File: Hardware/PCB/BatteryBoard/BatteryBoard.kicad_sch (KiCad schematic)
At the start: 16 parts

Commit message: wiring
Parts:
- added BT? (x2): BATT, symbol Device:Battery_Cell
- added C? (x2): 10u(3225), symbol Device:C_Small
- added C? (x2): 10u, symbol Device:C_Small
- added C?: 22u(3225), symbol Device:C_Small
- added C?: 4.7u, symbol Device:C_Small
- added C?: 47p, symbol Device:C_Small
- added C?: 0.047u, symbol Device:C_Small
- added C?: 0.47u, symbol Device:C_Small
- added D?: D_Schottky, symbol Device:D_Schottky
- added L?: 1uH, symbol Device:L_Small
- added R?: 330, symbol Device:R_Small
- added R? (x5): 4.7k, symbol Device:R_Small
- added R?: 10, symbol Device:R_Small
- added R?: 374, symbol Device:R_Small
- added U?: LT1963AEST-3.3, symbol Regulator_Linear:L7805
- added U?: NJM2396F05, symbol Regulator_extlib:NJM2396F05
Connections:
- net +BATT: now also U?.13 (BAT), U?.14 (BAT), BT?.1 (+), C?.1
- net GND: now also BT?.2 (-), C?.2, C?.2, C?.2, C?.2, C?.2, C?.2, C?.2, C?.2, R?.1, R?.1, U?.2 (GND), U?.3 (GND)
- net VBUS: now also R?.2, R?.2, R?.2, R?.2
- net PG: now reaches U?.1 (~{PG})
- net PG: now also R?.1
- net CBSET: now reaches U?.10 (CBSET)
- net CBSET: now also R?.2
- net at U?.11 (REGN): now also C?.1
- net at U?.12 (BTST): now also C?.1
- net at U?.15 (SNS): now also U?.16 (SNS), C?.1
- net SW: now reaches U?.17 (SW)
- net SW: now also U?.18 (SW), C?.2, L?.1
- net PMID: now reaches U?.21 (PMID)
- net PMID: now also U?.22 (PMID), C?.1, L?.2
- net PSEL: now reaches U?.24 (PSEL)
- net CD: now reaches U?.3 (CD)
- net SDA: now reaches U?.4 (SDA)
- net SDA: now also R?.1
- net SCL: now reaches U?.5 (SCL)
- net SCL: now also R?.1
- net INT: now reaches U?.6 (~{INT})
- net INT: now also R?.1
- net TS: now reaches U?.7 (TS)
- net at U?.8 (ILIM): now also R?.2
- net MID: now reaches U?.9 (MID)
- net MID: now also R?.2
- net at SW?.1 (A): now also R?.2
- net at SW?.2 (B): now also U?.4 (EN)
- net at SW?.3 (C): now also Q?.3 (D), C?.1, D?.1 (K), U?.1 (IN)
- net VDD renamed +5V
- net +5V: now also C?.1, C?.1, D?.2 (A), U?.1 (IN), U?.2 (OUT); no longer Q?.3 (D)
- new net: BT?.1 (+), BT?.2 (-), R?.1, R?.1
- new net +3.3V: C?.1, U?.3 (OUT)
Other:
- note added: "Charge"
- note added: "Interface"
- note added: "Regulator"
- note added: "USB接続時に0V"
- note added: "min:0V max:8.4V"
- note removed: "min:5V max:8.4V"
- moved on the sheet: C?, D?, J?, Q?, R?, SW?, U?

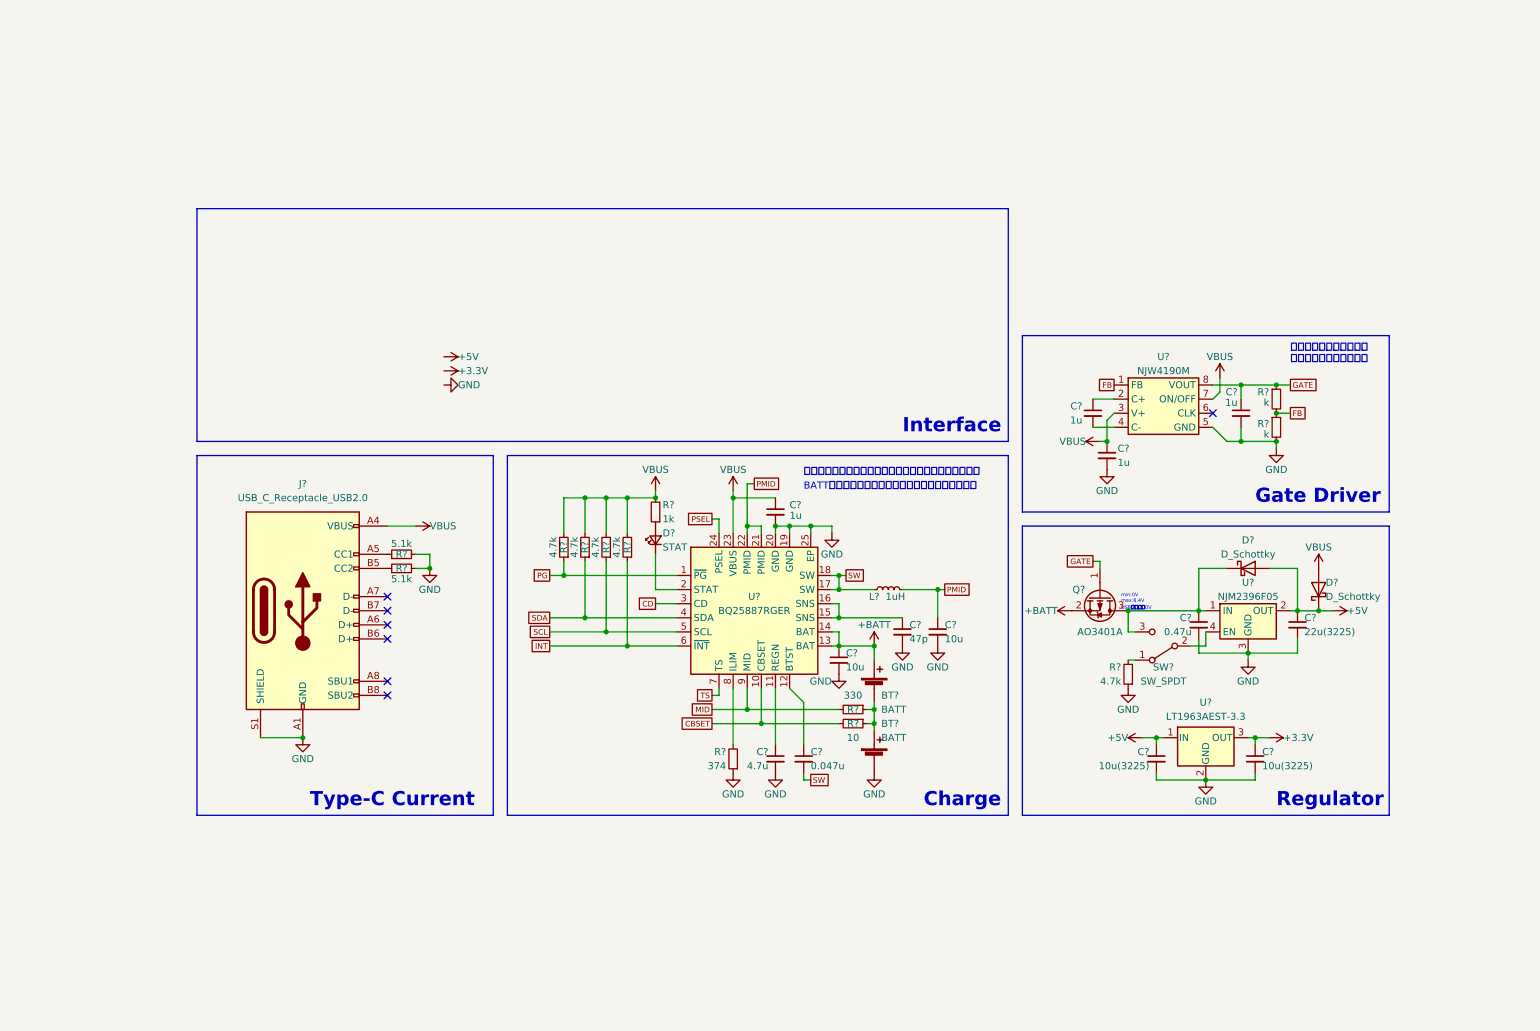
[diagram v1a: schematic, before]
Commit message: バッテリモジュールを設計中
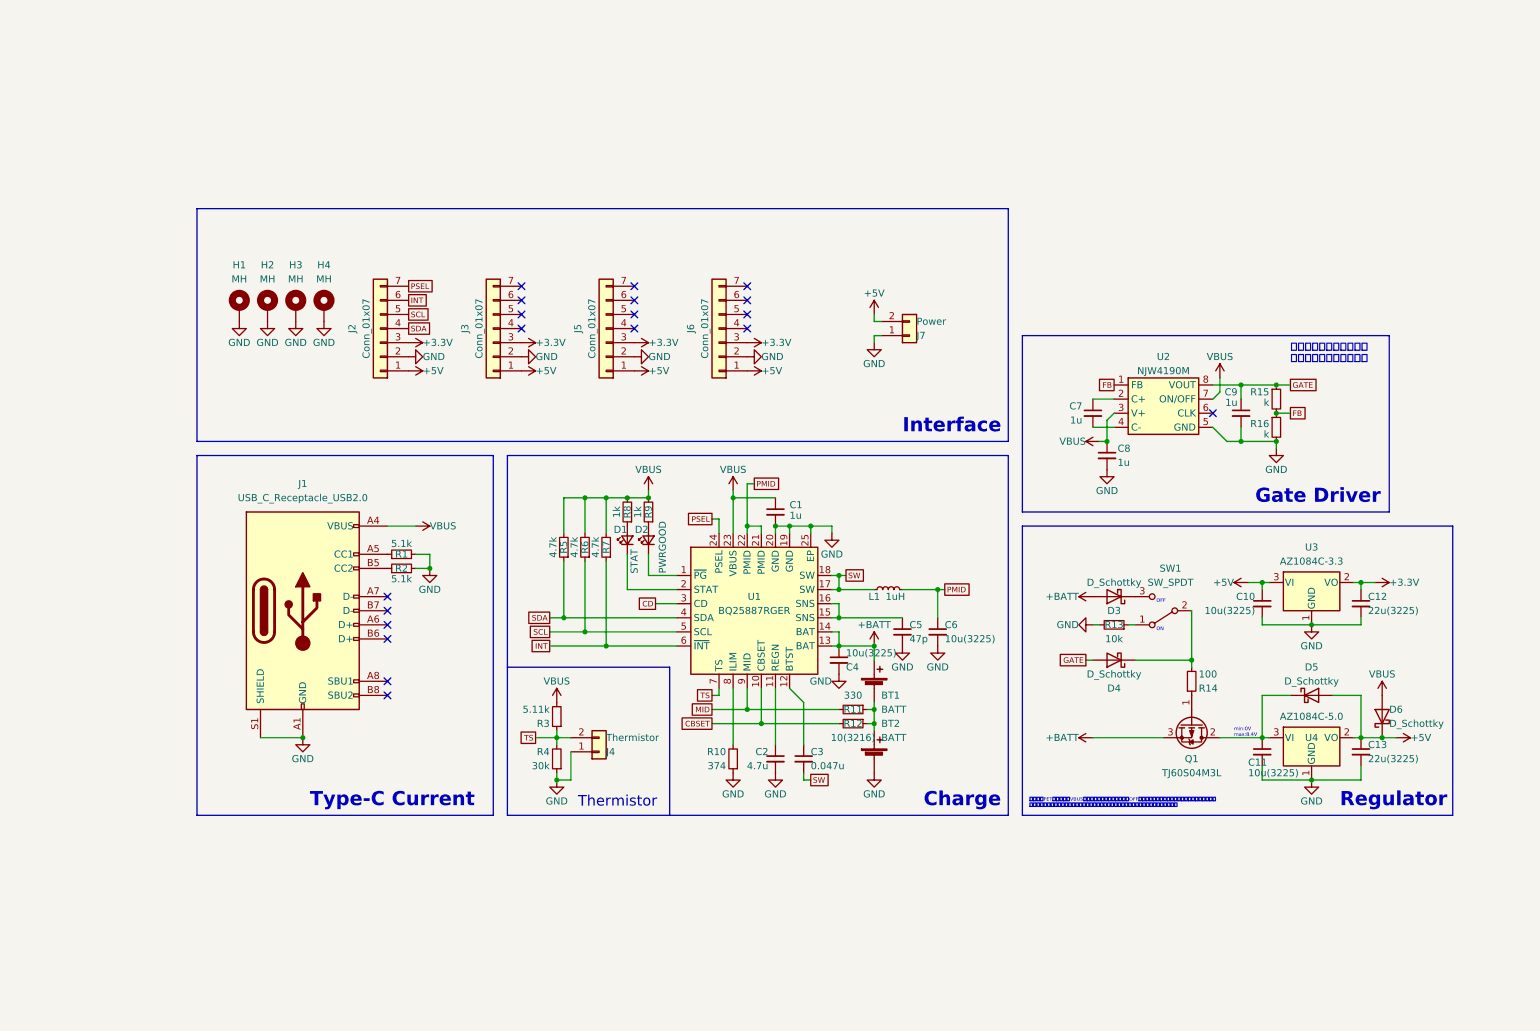
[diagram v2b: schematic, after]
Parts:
- removed C?: 0.47u, symbol Device:C_Small
- removed Q?: AO3401A, symbol Device:Q_PMOS_GSD
- removed R? (x2): 4.7k, symbol Device:R_Small
- removed U?: LT1963AEST-3.3, symbol Regulator_Linear:L7805
- removed U?: NJM2396F05, symbol Regulator_extlib:NJM2396F05
- added C11: 10u(3225), Capacitor_SMD:C_1210_3225Metric, symbol Device:C_Small
- added D2: PWRGOOD, LED_SMD:LED_0603_1608Metric, symbol Device:LED_Small
- added D3, D4: D_Schottky, CUHS20S30:CUHS20S30, symbol Device:D_Schottky
- added H1, H2, H3, H4: MH, MountingHole:MountingHole_2.2mm_M2_Pad_Via, symbol Mechanical:MountingHole_Pad
- added J2, J3, J5, J6: Conn_01x07, Connector_PinSocket_2.54mm:PinSocket_1x07_P2.54mm_Vertical, symbol Connector_Generic:Conn_01x07
- added J4: Thermistor, Connector_JST:JST_XH_B2B-XH-A_1x02_P2.50mm_Vertical, symbol Connector_Generic:Conn_01x02
- added J7: Power, Connector_AMASS:AMASS_XT30UPB-F_1x02_P5.0mm_Vertical, symbol Connector_Generic:Conn_01x02
- added Q1: TJ60S04M3L, Package_TO_SOT_SMD:TO-252-2, symbol Device:Q_PMOS_GDS
- added R13: 10k, Resistor_SMD:R_0603_1608Metric, symbol Device:R_Small
- added R14: 100, Resistor_SMD:R_0603_1608Metric, symbol Device:R_Small
- added R3: 5.11k, Resistor_SMD:R_0603_1608Metric, symbol Device:R_Small
- added R4: 30k, Resistor_SMD:R_0603_1608Metric, symbol Device:R_Small
- added R9: 1k, Resistor_SMD:R_0603_1608Metric, symbol Device:R_Small
- added U3: AZ1084C-3.3, Package_TO_SOT_SMD:TO-252-2, symbol Regulator_Linear:AZ1084-3.3
- added U4: AZ1084C-5.0, Package_TO_SOT_SMD:TO-252-2, symbol Regulator_Linear:AZ1084-5.0
- BT1, BT2: renamed from BT?; footprint (none) -> Battery_extlib:BatteryClip_Keystone_18500
- C1, C2, C3, C5, C7, C8, C9: renamed from C?; footprint (none) -> Capacitor_SMD:C_0603_1608Metric
- C10, C13: renamed from C?; footprint (none) -> Capacitor_SMD:C_1210_3225Metric
- C12: renamed from C?; value 10u(3225) -> 22u(3225); footprint (none) -> Capacitor_SMD:C_1210_3225Metric
- C4, C6: renamed from C?; value 10u -> 10u(3225); footprint (none) -> Capacitor_SMD:C_1210_3225Metric
- D1: renamed from D?; footprint (none) -> LED_SMD:LED_0603_1608Metric
- D5, D6: renamed from D?; footprint (none) -> CUHS20S30:CUHS20S30
- J1: renamed from J?; footprint (none) -> Kicad_Akiyuki_Footprint:CUI_UJC-HP-3-SMT-TR
- L1: renamed from L?; footprint (none) -> Inductor_SMD:L_1210_3225Metric
- R1, R10, R11, R15, R16, R2, R5, R6, R7, R8: renamed from R?; footprint (none) -> Resistor_SMD:R_0603_1608Metric
- R12: renamed from R?; value 10 -> 10(3216); footprint (none) -> Resistor_SMD:R_1206_3216Metric
- SW1: renamed from SW?; footprint (none) -> Button_Switch_THT_extlib:NKK_SS-12SDP2
- U1: renamed from U?; footprint (none) -> Package_DFN_QFN:VQFN-24-1EP_4x4mm_P0.5mm_EP2.45x2.45mm_ThermalVias
- U2: renamed from U?; footprint (none) -> Kicad_Akiyuki_Footprint:DMP-8_P1.27mm
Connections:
- net +3.3V: now also J2.3 (Pin_3), J3.3 (Pin_3), J5.3 (Pin_3), J6.3 (Pin_3), U3.2 (VO)
- net +5V: now also J2.1 (Pin_1), J3.1 (Pin_1), J5.1 (Pin_1), J6.1 (Pin_1), J7.2 (Pin_2), U3.3 (VI), U4.2 (VO)
- net +BATT: now also D3.2 (A), Q1.3 (S)
- net GATE: now also D4.2 (A)
- net GND: now also C11.2, H1.1, H2.1, H3.1, H4.1, J2.2 (Pin_2), J3.2 (Pin_2), J4.1 (Pin_1), J5.2 (Pin_2), J6.2 (Pin_2), J7.1 (Pin_1), R13.2, R4.1, U3.1 (GND), U4.1 (GND)
- net INT: now also J2.6 (Pin_6)
- net PSEL: now also J2.7 (Pin_7)
- net SCL: now also J2.5 (Pin_5)
- net SDA: now also J2.4 (Pin_4)
- net TS: now also J4.2 (Pin_2), R3.1, R4.2
- net VBUS: now also R3.2, R9.2
- net at D5.1 (K): now also C11.1, Q1.2 (D), U4.3 (VI); no longer SW1.3 (C)
- net at SW1.1 (A): now also R13.1
- net at SW1.2 (B): now also D4.1 (K), R14.2
- net PG: no longer names the net of U1.1 (~{PG})
- net PG: now also D2.1 (K)
- new net: D3.1 (K), SW1.3 (C)
- new net: D2.2 (A), R9.1
- new net: Q1.1 (G), R14.1
- no-connect marks 7 -> 19
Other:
- note added: "OFF"
- note added: "ON"
- note added: "Thermistor"
- note added: "２段目のFETが無いと、VBUSを繋いだとしてもスイッチをOFFにしない限りバッテリからの供給が止まらない。 つまり充電電流がそのまま出てくる。レギュレータの出力を弄っても消費電流があるので同様"
- note removed: "BATT側にスイッチ付けると、ソースが浮いてしまう"
- note removed: "USB接続時に0V"
- note removed: "システムへの供給は切っても充電はできるようにしたい"
- moved on the sheet: C10, C12, C13, D1, D5, D6, R5, R6, R7, R8, SW1

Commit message: 電源回路配置
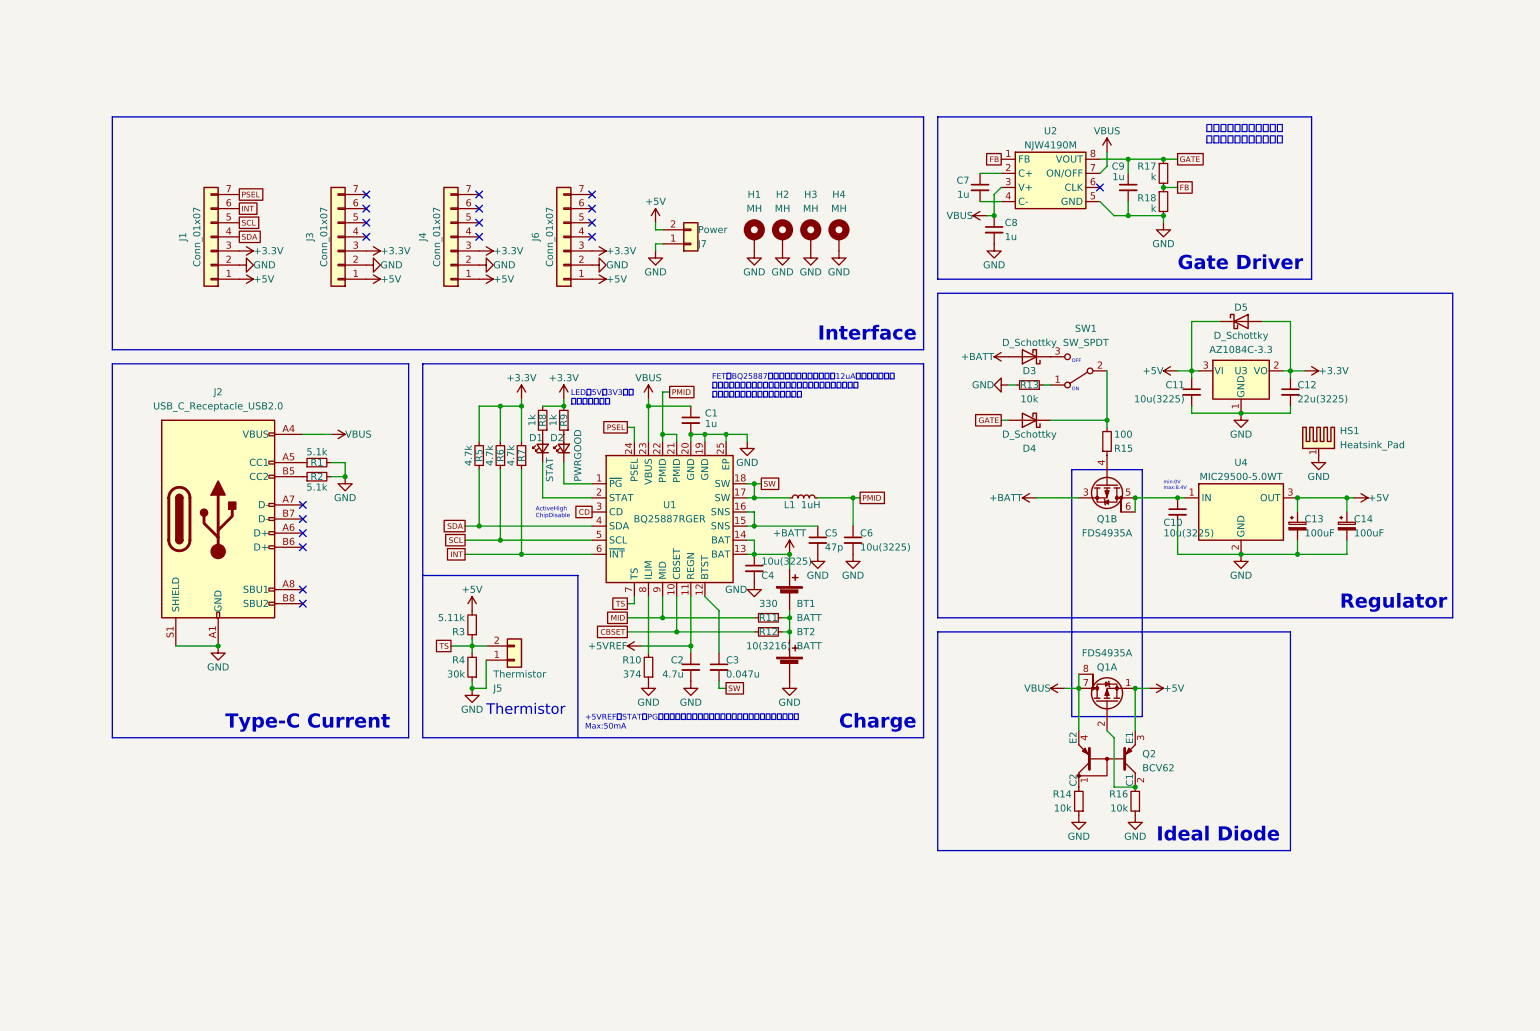
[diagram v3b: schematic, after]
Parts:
- removed C13: 22u(3225), Capacitor_SMD:C_1210_3225Metric, symbol Device:C_Small
- removed D6: D_Schottky, CUHS20S30:CUHS20S30, symbol Device:D_Schottky
- removed Q1: TJ60S04M3L, Package_TO_SOT_SMD:TO-252-2, symbol Device:Q_PMOS_GDS
- removed U4: AZ1084C-5.0, Package_TO_SOT_SMD:TO-252-2, symbol Regulator_Linear:AZ1084-5.0
- added C13, C14: 100uF, Capacitor_THT:CP_Radial_D5.0mm_P2.00mm, symbol Device:C_Polarized_Small
- added HS1: Heatsink_Pad, Heatsink_extlib:Heatsink_15x11mm_11PB015, symbol Mechanical:Heatsink_Pad
- added Q1: FDS4935A, Package_SO:SOIC-8_3.9x4.9mm_P1.27mm, symbol Device:Q_Dual_PMOS_S1G1S2G2D2D2D1D1
- added Q2: BCV62, Package_TO_SOT_SMD:SOT-143, symbol Device:Q_Dual_PNP_C2C1E1E2
- added R14, R16: 10k, Resistor_SMD:R_0603_1608Metric, symbol Device:R_Small
- added U4: MIC29500-5.0WT, Package_TO_SOT_THT:TO-220-3_Vertical, symbol Regulator_Linear:LT1963AxST-3.3
- renumbered C11 to C10, C10 to C11, J2 to J1, J1 to J2, J5 to J4, J4 to J5, R14 to R15, R15 to R17, R16 to R18
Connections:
- net +3.3V: now also D5.2 (A), R5.2, R6.2, R7.2, R8.2, R9.2
- net +5V: now also D5.1 (K), R3.2, C13.1, C14.1, Q1.1 (S), Q2.3 (E1), U4.3 (OUT); no longer D5.2 (A)
- net +BATT: now also Q1.3 (S)
- net GND: now also C13.2, C14.2, HS1.1, R14.1, R16.1, U4.2 (GND)
- net VBUS: now also Q1.7 (D), Q1.8 (G), Q2.4 (E2); no longer R3.2, R5.2, R6.2, R7.2, R8.2, R9.2
- net at C10.1: now also Q1.5 (D), Q1.6 (G), U4.1 (IN); no longer D5.1 (K)
- net +5VREF: now reaches C2.1, U1.11 (REGN)
- net at R15.1: now also Q1.4 (G)
- new net: Q2.1 (C2), R14.2
- new net: Q1.2 (G), Q2.2 (C1), R16.2
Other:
- note added: "+5VREFはSTATとPGのプルアップとサーミスタに使えるが、敢えて使わない Max:50mA"
- note added: "ActiveHigh ChipDisable"
- note added: "FETでBQ25887とバッテリの接続を切ると12uAを節約できるが ボディダイオードの順方向電圧のために充電できなくなる 理想ダイオードを追加しても怪しい"
- note added: "Ideal Diode"
- note added: "LEDが5Vか3V3かは 配線して決める"
- note removed: "２段目のFETが無いと、VBUSを繋いだとしてもスイッチをOFFにしない限りバッテリからの供給が止まらない。 つまり充電電流がそのまま出てくる。レギュレータの出力を弄っても消費電流があるので同様"
- moved on the sheet: BT1, BT2, C1, C10, C11, C12, C2, C3, C4, C5, C6, C7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
